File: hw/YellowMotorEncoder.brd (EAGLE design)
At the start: 35 x 22.4 mm, 20 parts, among them P1 M1

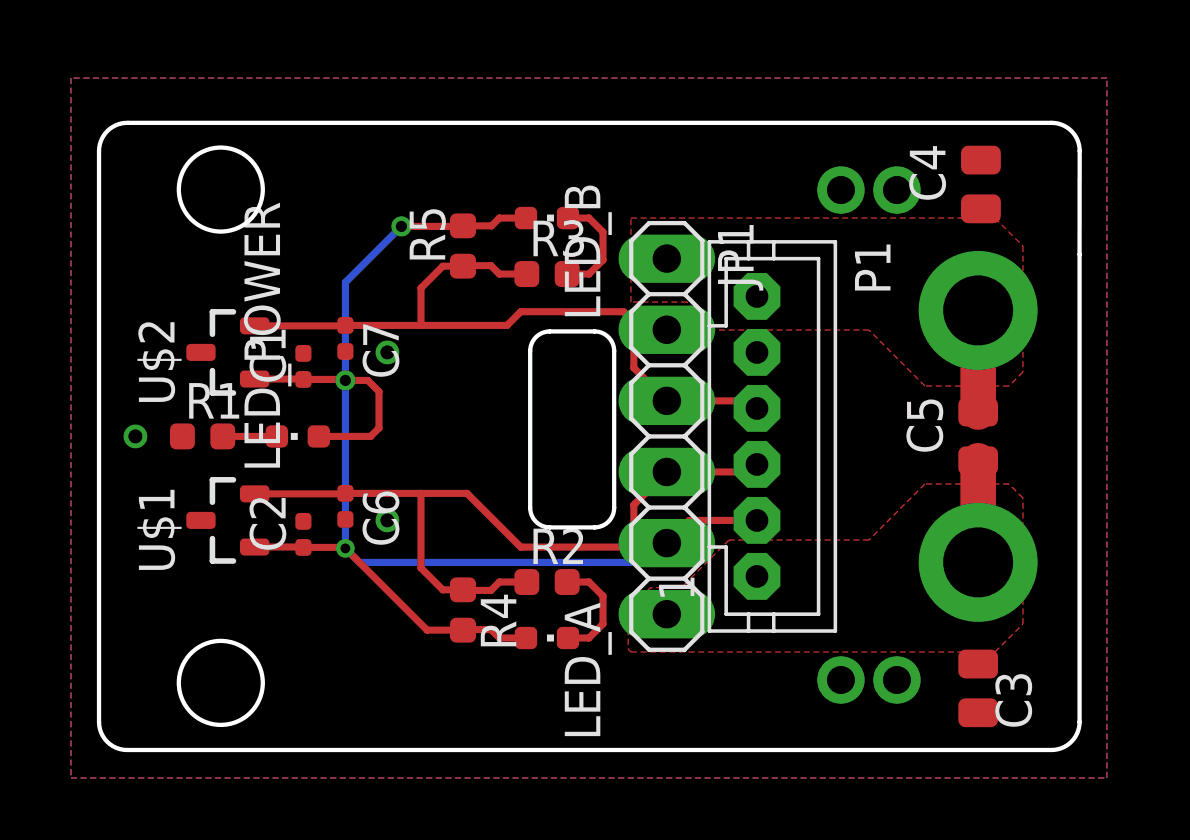
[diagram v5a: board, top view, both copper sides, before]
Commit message: Improve layout for manufacturing
- add JLC order number to silkscreen
- add JLC tooling holes
- fix rotation of hall sensors (`hall_sensor.lbr`)
- decrease size of silkscreen text- board name, version, licence and URL
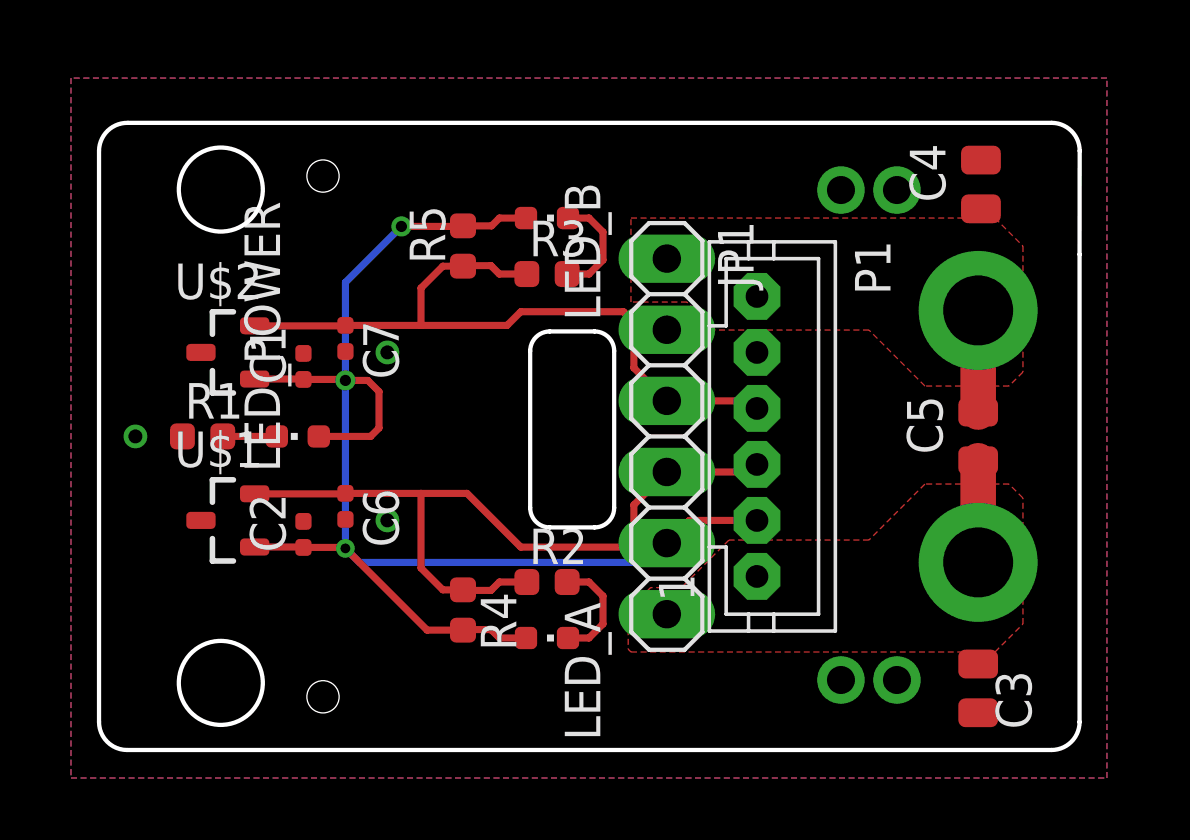
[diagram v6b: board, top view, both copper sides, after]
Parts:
- turned U$1 to 0 degrees
- turned U$2 to 0 degrees
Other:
- board text added: "JLCJLCJLCJLC"
- board text added: "RB0003-YellowMotorEncoder"
- board text added: "github::roboticsbrno/"
- board text removed: "github::roboticsbrno/ RB0003-YellowMotorEncoder"
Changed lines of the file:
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@@
 <?xml version="1.0" encoding="utf-8"?>
 <!DOCTYPE eagle SYSTEM "eagle.dtd">
-<eagle version="9.6.1">
+<eagle version="9.6.0">
 <drawing>
 <settings>
@@
 <layer number="43" name="vRestrict" color="2" fill="10" visible="yes" active="yes"/>
 <layer number="44" name="Drills" color="7" fill="1" visible="no" active="yes"/>
-<layer number="45" name="Holes" color="7" fill="1" visible="no" active="yes"/>
+<layer number="45" name="Holes" color="7" fill="1" visible="yes" active="yes"/>
 <layer number="46" name="Milling" color="3" fill="1" visible="no" active="yes"/>
 <layer number="47" name="Measures" color="7" fill="1" visible="no" active="yes"/>
@@
 VCC
 M+</text>
-<text x="9.5" y="21" size="1" layer="51" font="vector" ratio="20">YellowMotorEncoder</text>
-<text x="9.5" y="19.8" size="1" layer="51" font="vector" ratio="20">v1.0 CC BY-SA 4.0</text>
-<text x="6.852" y="2.952" size="1" layer="51" font="vector" ratio="20" align="top-left">github::roboticsbrno/
-RB0003-YellowMotorEncoder</text>
+<text x="10.5" y="21.4" size="0.8128" layer="51" font="vector" ratio="20">YellowMotorEncoder</text>
+<text x="10.5" y="20.1" size="0.8128" layer="51" font="vector" ratio="20">v1.0 CC BY-SA 4.0</text>
+<text x="10.652" y="2.452" size="0.8128" layer="51" font="vector" ratio="20" align="top-left">github::roboticsbrno/</text>
 <circle x="4.35" y="20.0173" radius="1.5" width="0.1524" layer="20"/>
 <wire x1="16.1" y1="14.95" x2="15.4" y2="14.25" width="0.1524" layer="20" curve="89.9997"/>
@@
 <rectangle x1="25.5" y1="19" x2="30.4" y2="21.6" layer="29"/>
 <rectangle x1="25.4" y1="1.3" x2="30.4" y2="3.6" layer="29"/>
+<hole x="8" y="20.5" drill="1.152"/>
+<hole x="8" y="1.9" drill="1.152"/>
+<text x="10.652" y="1.052" size="0.8128" layer="51" font="vector" ratio="20" align="top-left">RB0003-YellowMotorEncoder</text>
+<text x="25.553" y="11.329" size="1" layer="51" font="vector" ratio="20" rot="R90" align="bottom-center">JLCJLCJLCJLC</text>
 </plain>
 <attributes>
@@
 <attribute name="NAME" x="27.0001" y="18.2" size="1.27" layer="25" rot="R270"/>
 </element>
-<element name="U$1" library="hall_sensor" package="SOT23" package3d_urn="urn:adsk.eagle:package:43389/2" value="MH253ESO" x="4.6" y="8.2" smashed="yes" rot="R90">
-<attribute name="EXTENDED" value="YES" x="4.6" y="8.2" size="1.778" layer="27" rot="R90" display="off"/>
-<attribute name="LCSC_ID" value="C114369" x="4.6" y="8.2" size="1.778" layer="27" rot="R90" display="off"/>
-<attribute name="MF" value="Magnesensor Tech (MST)" x="4.6" y="8.2" size="1.778" layer="27" rot="R90" display="off"/>
-<attribute name="MF_ID" value="MH253ESO" x="4.6" y="8.2" size="1.778" layer="27" rot="R90" display="off"/>
-<attribute name="NAME" x="2.695" y="6.295" size="1.27" layer="25" rot="R90"/>
-<attribute name="PACKAGE" value="SOT-23-3L" x="4.6" y="8.2" size="1.778" layer="27" rot="R90" display="off"/>
-<attribute name="PADS" value="3" x="4.6" y="8.2" size="1.778" layer="27" rot="R90" display="off"/>
-<attribute name="PRICE_1000PLUS" value="0.0889" x="4.6" y="8.2" size="1.778" layer="27" rot="R90" display="off"/>
-<attribute name="PRICE_100PLUS" value="0.0929" x="4.6" y="8.2" size="1.778" layer="27" rot="R90" display="off"/>
-<attribute name="PRICE_10PLUS" value="0.1049" x="4.6" y="8.2" size="1.778" layer="27" rot="R90" display="off"/>
-<attribute name="PRICE_1PLUS" value="0.1375" x="4.6" y="8.2" size="1.778" layer="27" rot="R90" display="off"/>
-<attribute name="PRICE_DATE" value="2020-05-01" x="4.6" y="8.2" size="1.778" layer="27" rot="R90" display="off"/>
-<attribute name="VALUE" x="7.775" y="6.295" size="1.27" layer="27" rot="R90"/>
-</element>
-<element name="U$2" library="hall_sensor" package="SOT23" package3d_urn="urn:adsk.eagle:package:43389/2" value="MH253ESO" x="4.6" y="14.2" smashed="yes" rot="R90">
-<attribute name="EXTENDED" value="YES" x="4.6" y="14.2" size="1.778" layer="27" rot="R90" display="off"/>
-<attribute name="LCSC_ID" value="C114369" x="4.6" y="14.2" size="1.778" layer="27" rot="R90" display="off"/>
-<attribute name="MF" value="Magnesensor Tech (MST)" x="4.6" y="14.2" size="1.778" layer="27" rot="R90" display="off"/>
-<attribute name="MF_ID" value="MH253ESO" x="4.6" y="14.2" size="1.778" layer="27" rot="R90" display="off"/>
-<attribute name="NAME" x="2.695" y="12.295" size="1.27" layer="25" rot="R90"/>
-<attribute name="PACKAGE" value="SOT-23-3L" x="4.6" y="14.2" size="1.778" layer="27" rot="R90" display="off"/>
-<attribute name="PADS" value="3" x="4.6" y="14.2" size="1.778" layer="27" rot="R90" display="off"/>
-<attribute name="PRICE_1000PLUS" value="0.0889" x="4.6" y="14.2" size="1.778" layer="27" rot="R90" display="off"/>
-<attribute name="PRICE_100PLUS" value="0.0929" x="4.6" y="14.2" size="1.778" layer="27" rot="R90" display="off"/>
-<attribute name="PRICE_10PLUS" value="0.1049" x="4.6" y="14.2" size="1.778" layer="27" rot="R90" display="off"/>
-<attribute name="PRICE_1PLUS" value="0.1375" x="4.6" y="14.2" size="1.778" layer="27" rot="R90" display="off"/>
-<attribute name="PRICE_DATE" value="2020-05-01" x="4.6" y="14.2" size="1.778" layer="27" rot="R90" display="off"/>
-<attribute name="VALUE" x="7.775" y="12.295" size="1.27" layer="27" rot="R90"/>
+<element name="U$1" library="hall_sensor" package="SOT23" package3d_urn="urn:adsk.eagle:package:43389/2" value="MH253ESO" x="4.6" y="8.2" smashed="yes">
+<attribute name="EXTENDED" value="YES" x="4.6" y="8.2" size="1.778" layer="27" display="off"/>
+<attribute name="LCSC_ID" value="C114369" x="4.6" y="8.2" size="1.778" layer="27" display="off"/>
+<attribute name="MF" value="Magnesensor Tech (MST)" x="4.6" y="8.2" size="1.778" layer="27" display="off"/>
+<attribute name="MF_ID" value="MH253ESO" x="4.6" y="8.2" size="1.778" layer="27" display="off"/>
+<attribute name="NAME" x="2.695" y="10.105" size="1.27" layer="25"/>
+<attribute name="PACKAGE" value="SOT-23-3L" x="4.6" y="8.2" size="1.778" layer="27" display="off"/>
+<attribute name="PADS" value="3" x="4.6" y="8.2" size="1.778" layer="27" display="off"/>
+<attribute name="PRICE_1000PLUS" value="0.0889" x="4.6" y="8.2" size="1.778" layer="27" display="off"/>
+<attribute name="PRICE_100PLUS" value="0.0929" x="4.6" y="8.2" size="1.778" layer="27" display="off"/>
+<attribute name="PRICE_10PLUS" value="0.1049" x="4.6" y="8.2" size="1.778" layer="27" display="off"/>
+<attribute name="PRICE_1PLUS" value="0.1375" x="4.6" y="8.2" size="1.778" layer="27" display="off"/>
+<attribute name="PRICE_DATE" value="2020-05-01" x="4.6" y="8.2" size="1.778" layer="27" display="off"/>
+<attribute name="VALUE" x="2.695" y="5.025" size="1.27" layer="27"/>
+</element>
+<element name="U$2" library="hall_sensor" package="SOT23" package3d_urn="urn:adsk.eagle:package:43389/2" value="MH253ESO" x="4.6" y="14.2" smashed="yes">
+<attribute name="EXTENDED" value="YES" x="4.6" y="14.2" size="1.778" layer="27" display="off"/>
+<attribute name="LCSC_ID" value="C114369" x="4.6" y="14.2" size="1.778" layer="27" display="off"/>
+<attribute name="MF" value="Magnesensor Tech (MST)" x="4.6" y="14.2" size="1.778" layer="27" display="off"/>
+<attribute name="MF_ID" value="MH253ESO" x="4.6" y="14.2" size="1.778" layer="27" display="off"/>
+<attribute name="NAME" x="2.695" y="16.105" size="1.27" layer="25"/>
+<attribute name="PACKAGE" value="SOT-23-3L" x="4.6" y="14.2" size="1.778" layer="27" display="off"/>
+<attribute name="PADS" value="3" x="4.6" y="14.2" size="1.778" layer="27" display="off"/>
+<attribute name="PRICE_1000PLUS" value="0.0889" x="4.6" y="14.2" size="1.778" layer="27" display="off"/>
+<attribute name="PRICE_100PLUS" value="0.0929" x="4.6" y="14.2" size="1.778" layer="27" display="off"/>
+<attribute name="PRICE_10PLUS" value="0.1049" x="4.6" y="14.2" size="1.778" layer="27" display="off"/>
+<attribute name="PRICE_1PLUS" value="0.1375" x="4.6" y="14.2" size="1.778" layer="27" display="off"/>
+<attribute name="PRICE_DATE" value="2020-05-01" x="4.6" y="14.2" size="1.778" layer="27" display="off"/>
+<attribute name="VALUE" x="2.695" y="11.025" size="1.27" layer="27"/>
 </element>
 <element name="LED_A" library="led" package="CHIPLED_0603" package3d_urn="urn:adsk.eagle:package:15822/2" value="RED" x="16" y="4" smashed="yes" rot="R180">

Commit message: Add and move motor polygons
- add bottom polygons for motor pins/soldering holes
- move unmask polygons for motor pads to not overlap with M+/M-
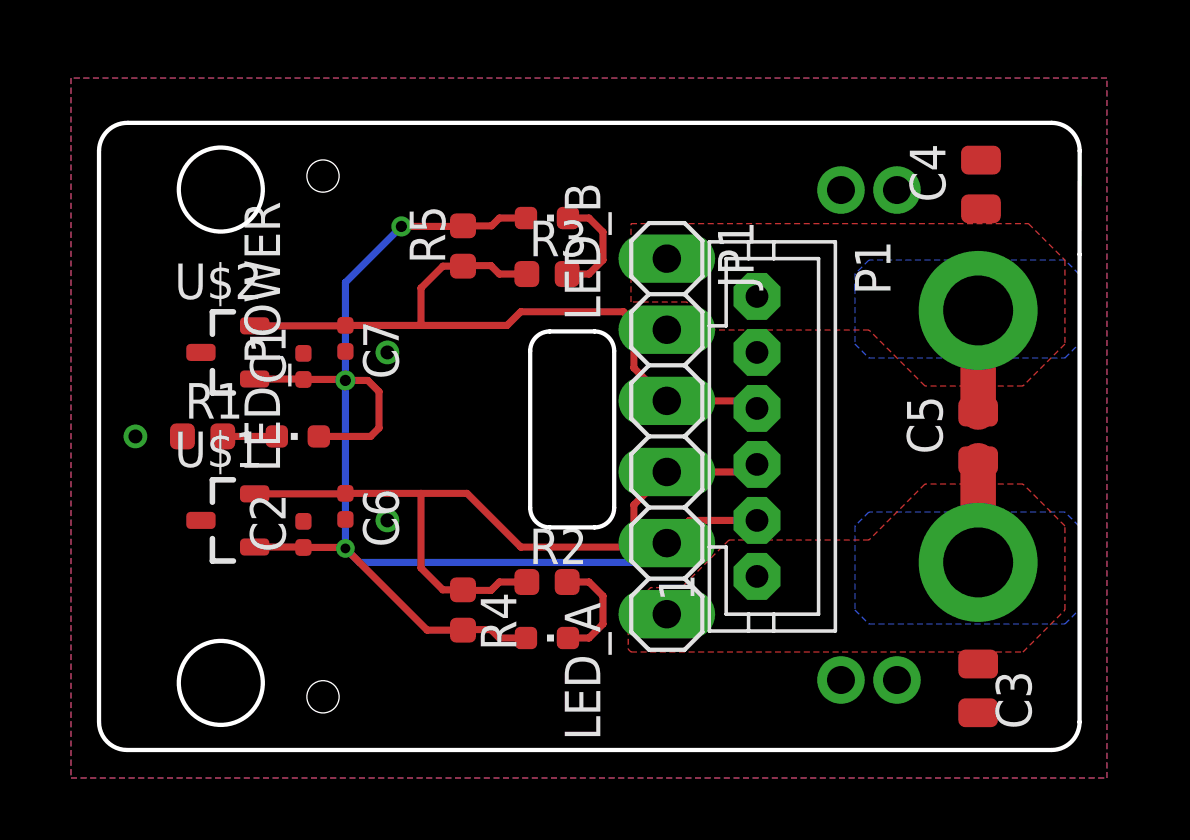
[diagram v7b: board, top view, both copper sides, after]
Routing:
- added copper zone on layer 16, net M+
- added copper zone on layer 16, net M-
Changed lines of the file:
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@@
 <drawing>
 <settings>
-<setting alwaysvectorfont="no"/>
+<setting alwaysvectorfont="yes"/>
 <setting verticaltext="up"/>
 </settings>
@@
 VCC
 M+</text>
-<rectangle x1="25.5" y1="19" x2="30.4" y2="21.6" layer="29"/>
-<rectangle x1="25.4" y1="1.3" x2="30.4" y2="3.6" layer="29"/>
+<rectangle x1="25.4" y1="19.3" x2="30.3" y2="21.6" layer="29"/>
+<rectangle x1="25.3" y1="0.7" x2="30.2" y2="3" layer="29"/>
 <hole x="8" y="20.5" drill="1.152"/>
 <hole x="8" y="1.9" drill="1.152"/>
@@
 <wire x1="31.4" y1="12.07" x2="31.4" y2="15.7" width="1.27" layer="1"/>
 <polygon width="0.4064" layer="1" rank="2">
-<vertex x="19" y="19"/>
-<vertex x="32" y="19"/>
-<vertex x="33" y="18"/>
-<vertex x="33" y="13.5"/>
-<vertex x="32.5" y="13"/>
+<vertex x="19" y="18.8"/>
+<vertex x="33.2" y="18.8"/>
+<vertex x="34.5" y="17.5"/>
+<vertex x="34.5" y="14.5"/>
+<vertex x="33" y="13"/>
 <vertex x="29.5" y="13"/>
 <vertex x="27.5" y="15"/>
@@
 <vertex x="19" y="16"/>
 </polygon>
+<polygon width="0.1524" layer="16">
+<vertex x="27" y="16.5"/>
+<vertex x="27" y="14.5"/>
+<vertex x="27.5" y="14"/>
+<vertex x="34.5" y="14"/>
+<vertex x="35" y="14.5"/>
+<vertex x="35" y="16.5"/>
+<vertex x="35" y="17"/>
+<vertex x="34.5" y="17.5"/>
+<vertex x="28" y="17.5"/>
+<vertex x="27.5" y="17.5"/>
+<vertex x="27" y="17"/>
+</polygon>
+<wire x1="31.4" y1="15.7" x2="31.5" y2="19.33" width="0" layer="19" extent="1-1"/>
 </signal>
 <signal name="M+">
@@
 <vertex x="18.9" y="3.6"/>
 <vertex x="19" y="3.5"/>
-<vertex x="32" y="3.5"/>
-<vertex x="33" y="4.5"/>
-<vertex x="33" y="9"/>
-<vertex x="32.5" y="9.5"/>
+<vertex x="33" y="3.5"/>
+<vertex x="34.5" y="5"/>
+<vertex x="34.5" y="8"/>
+<vertex x="33" y="9.5"/>
 <vertex x="29.5" y="9.5"/>
 <vertex x="27.5" y="7.5"/>
@@
 <vertex x="20.8" y="5.8"/>
 </polygon>
+<polygon width="0.1524" layer="16">
+<vertex x="34.5" y="8.5"/>
+<vertex x="27.5" y="8.5"/>
+<vertex x="27" y="8"/>
+<vertex x="27" y="5"/>
+<vertex x="27.5" y="4.5"/>
+<vertex x="34.5" y="4.5"/>
+<vertex x="35" y="5"/>
+<vertex x="35" y="8"/>
+</polygon>
 </signal>
